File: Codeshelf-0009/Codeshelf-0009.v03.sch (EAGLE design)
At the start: 24 parts, among them U1 MC9S08QG-DT, U2 LED5060A, U3 RS485SOIC, U4 CAT9552

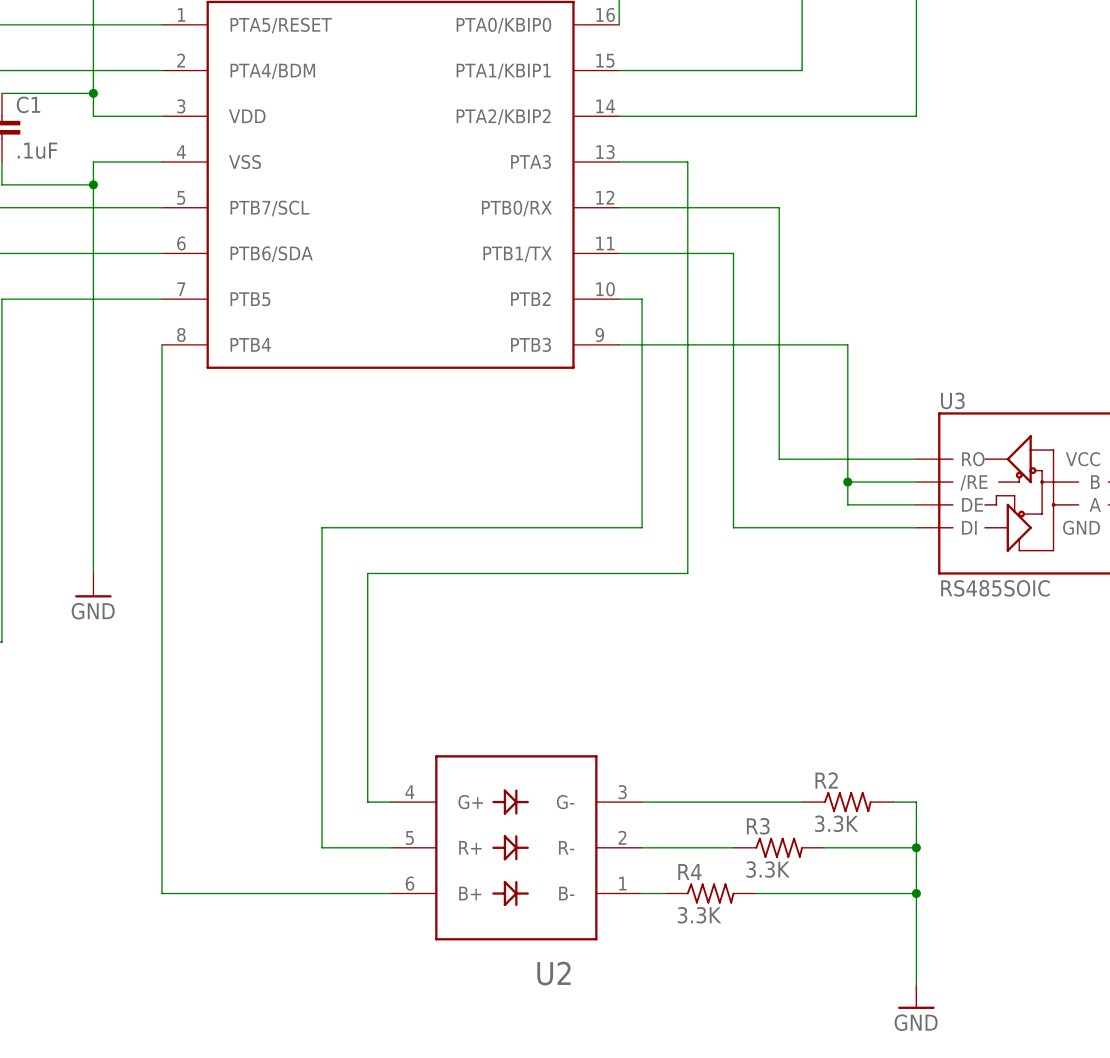
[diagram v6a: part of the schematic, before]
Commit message: Switched LED
Exchanged for WS2812 and reroute to match old PosCon pin assigments for
firmware compatibility.
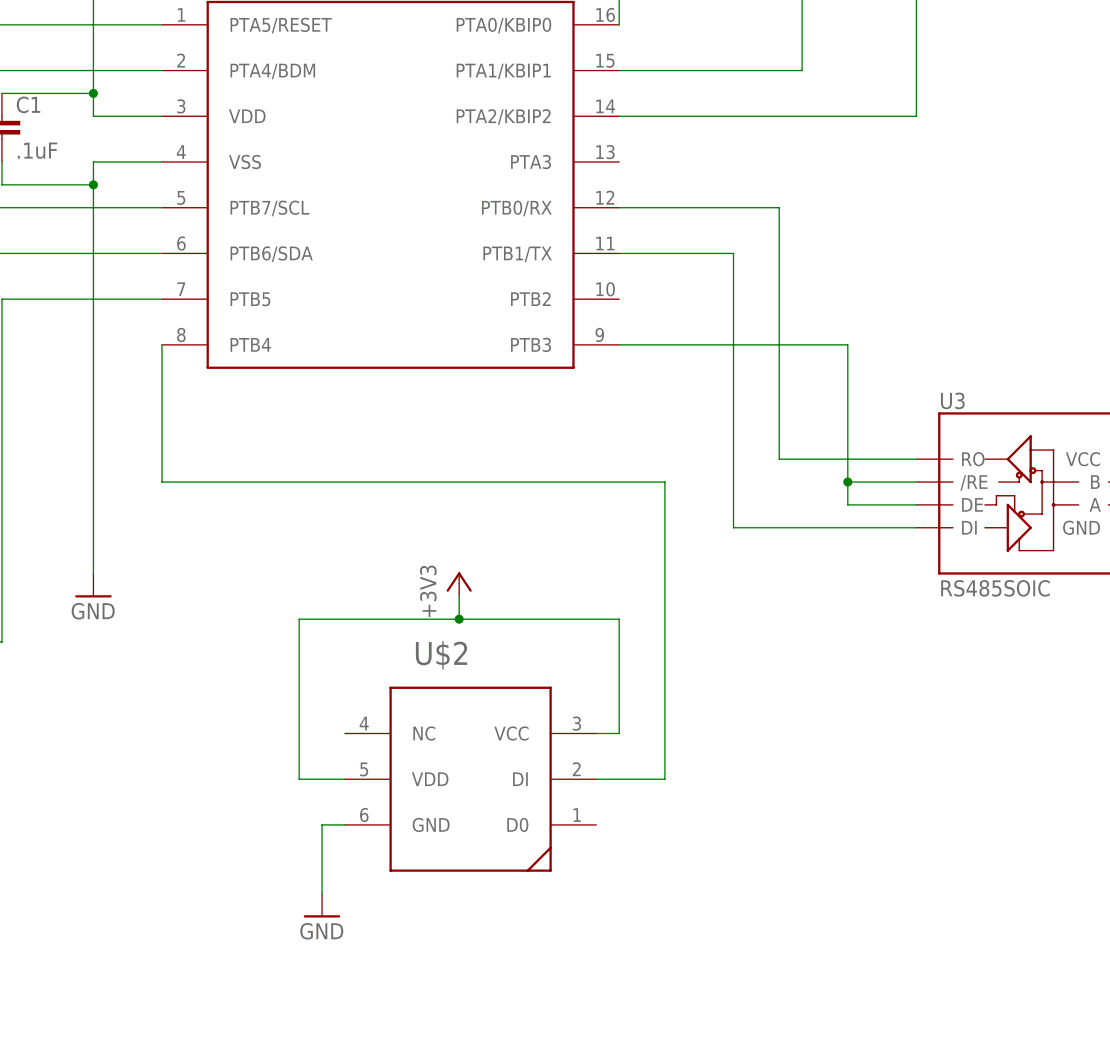
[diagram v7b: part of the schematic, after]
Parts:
- removed R2, R3, R4: 3.3K, GW-devices:RF-R0402
- removed U2: LED5060A, GW-devices:LED5060A
- added U$2: WS2812, GW-devices:WS2812
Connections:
- removed net N$1: R2.1, U2.G-
- removed net N$4: R4.1, U2.B-
- removed net N$5: U1.PTA3, U2.G+
- removed net N$6: U1.PTB2, U2.R+
- removed net N$7: U1.PTB4, U2.B+
- net +3V3: now also U$2.VCC, U$2.VDD
- net GND: now also U$2.GND; no longer R2.2, R3.2, R4.2
- net N$3: now also U$2.DI, U1.PTB4; no longer R3.1, U2.R-
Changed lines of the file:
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@@
 <attribute name="PRICE" value="4.29"/>
 </part>
-<part name="U2" library="GW-devices" deviceset="LED5060" device="A"/>
-<part name="R2" library="GW-devices" deviceset="RF-R" device="0402" value="3.3K">
-<attribute name="MFGN" value="Panasonic"/>
-<attribute name="MFGP" value="ERJ-2GEJ332X"/>
-<attribute name="PRICE" value="0.02"/>
-</part>
-<part name="R3" library="GW-devices" deviceset="RF-R" device="0402" value="3.3K">
-<attribute name="MFGN" value="Panasonic"/>
-<attribute name="MFGP" value="ERJ-2GEJ332X"/>
-<attribute name="PRICE" value="0.02"/>
-</part>
-<part name="R4" library="GW-devices" deviceset="RF-R" device="0402" value="3.3K">
-<attribute name="MFGN" value="Panasonic"/>
-<attribute name="MFGP" value="ERJ-2GEJ332X"/>
-<attribute name="PRICE" value="0.02"/>
-</part>
-<part name="GND2" library="supply1" deviceset="GND" device=""/>
 <part name="U4" library="GW-devices" deviceset="CAT9552" device=""/>
 <part name="GND12" library="supply1" deviceset="GND" device=""/>
@@
 <part name="U$1" library="GW-devices" deviceset="RJ45-8" device=""/>
 <part name="U$2-PROG" library="GW-devices" deviceset="RJ45-8" device=""/>
+<part name="U$2" library="GW-devices" deviceset="WS2812" device=""/>
+<part name="GND2" library="supply1" deviceset="GND" device=""/>
+<part name="+3V7" library="supply1" deviceset="+3V3" device=""/>
 </parts>
 <sheets>
@@
 <attribute name="PRICE" x="68.58" y="-33.02" size="1.778" layer="96" display="off"/>
 </instance>
-<instance part="U2" gate="G$1" x="15.24" y="-73.66" rot="R180"/>
-<instance part="R2" gate="G$1" x="50.8" y="-68.58">
-<attribute name="MFGN" x="50.8" y="-68.58" size="1.778" layer="96" display="off"/>
-<attribute name="MFGP" x="50.8" y="-68.58" size="1.778" layer="96" display="off"/>
-<attribute name="PRICE" x="50.8" y="-68.58" size="1.778" layer="96" display="off"/>
-</instance>
-<instance part="R3" gate="G$1" x="43.18" y="-73.66">
-<attribute name="MFGN" x="43.18" y="-73.66" size="1.778" layer="96" display="off"/>
-<attribute name="MFGP" x="43.18" y="-73.66" size="1.778" layer="96" display="off"/>
-<attribute name="PRICE" x="43.18" y="-73.66" size="1.778" layer="96" display="off"/>
-</instance>
-<instance part="R4" gate="G$1" x="35.56" y="-78.74">
-<attribute name="MFGN" x="35.56" y="-78.74" size="1.778" layer="96" display="off"/>
-<attribute name="MFGP" x="35.56" y="-78.74" size="1.778" layer="96" display="off"/>
-<attribute name="PRICE" x="35.56" y="-78.74" size="1.778" layer="96" display="off"/>
-</instance>
-<instance part="GND2" gate="1" x="58.42" y="-91.44"/>
 <instance part="U4" gate="G$1" x="-134.62" y="81.28" rot="R270"/>
 <instance part="GND12" gate="1" x="-111.76" y="111.76" rot="R180"/>
@@
 <instance part="U$1" gate="G$1" x="170.18" y="-20.32"/>
 <instance part="U$2-PROG" gate="G$1" x="170.18" y="-66.04"/>
+<instance part="U$2" gate="G$1" x="10.16" y="-66.04"/>
+<instance part="GND2" gate="1" x="-7.62" y="-81.28"/>
+<instance part="+3V7" gate="G$1" x="7.62" y="-43.18"/>
 </instances>
 <busses>
@@
 <pinref part="BDM" gate="G$1" pin="8"/>
 <wire x1="-83.82" y1="25.4" x2="-71.12" y2="25.4" width="0.1524" layer="91"/>
-</segment>
-<segment>
-<wire x1="55.88" y1="-68.58" x2="58.42" y2="-68.58" width="0.1524" layer="91"/>
-<wire x1="58.42" y1="-68.58" x2="58.42" y2="-73.66" width="0.1524" layer="91"/>
-<wire x1="58.42" y1="-73.66" x2="58.42" y2="-78.74" width="0.1524" layer="91"/>
-<wire x1="58.42" y1="-78.74" x2="58.42" y2="-88.9" width="0.1524" layer="91"/>
-<wire x1="48.26" y1="-73.66" x2="58.42" y2="-73.66" width="0.1524" layer="91"/>
-<wire x1="40.64" y1="-78.74" x2="58.42" y2="-78.74" width="0.1524" layer="91"/>
-<junction x="58.42" y="-73.66"/>
-<junction x="58.42" y="-78.74"/>
-<pinref part="R2" gate="G$1" pin="2"/>
-<pinref part="GND2" gate="1" pin="GND"/>
-<pinref part="R3" gate="G$1" pin="2"/>
-<pinref part="R4" gate="G$1" pin="2"/>
 </segment>
 <segment>
@@
 <pinref part="U$4" gate="G$1" pin="4"/>
 </segment>
+<segment>
+<pinref part="U$2" gate="G$1" pin="GND"/>
+<pinref part="GND2" gate="1" pin="GND"/>
+<wire x1="-5.08" y1="-71.12" x2="-7.62" y2="-71.12" width="0.1524" layer="91"/>
+<wire x1="-7.62" y1="-71.12" x2="-7.62" y2="-78.74" width="0.1524" layer="91"/>
+</segment>
 </net>
 <net name="+3V3" class="1">
@@
 <wire x1="-307.34" y1="104.14" x2="-307.34" y2="106.68" width="0.1524" layer="91"/>
 </segment>
+<segment>
+<pinref part="U$2" gate="G$1" pin="VDD"/>
+<wire x1="-5.08" y1="-66.04" x2="-10.16" y2="-66.04" width="0.1524" layer="91"/>
+<wire x1="-10.16" y1="-66.04" x2="-10.16" y2="-48.26" width="0.1524" layer="91"/>
+<wire x1="-10.16" y1="-48.26" x2="7.62" y2="-48.26" width="0.1524" layer="91"/>
+<wire x1="7.62" y1="-48.26" x2="25.4" y2="-48.26" width="0.1524" layer="91"/>
+<wire x1="25.4" y1="-48.26" x2="25.4" y2="-60.96" width="0.1524" layer="91"/>
+<pinref part="U$2" gate="G$1" pin="VCC"/>
+<wire x1="25.4" y1="-60.96" x2="22.86" y2="-60.96" width="0.1524" layer="91"/>
+<pinref part="+3V7" gate="G$1" pin="+3V3"/>
+<wire x1="7.62" y1="-45.72" x2="7.62" y2="-48.26" width="0.1524" layer="91"/>
+<junction x="7.62" y="-48.26"/>
+</segment>
 </net>
 <net name="TX" class="0">
@@
 <pinref part="U$1" gate="G$1" pin="5"/>
 <pinref part="U$2-PROG" gate="G$1" pin="5"/>
-</segment>
-</net>
-<net name="N$1" class="0">
-<segment>
-<wire x1="27.94" y1="-68.58" x2="45.72" y2="-68.58" width="0.1524" layer="91"/>
-<pinref part="U2" gate="G$1" pin="G-"/>
-<pinref part="R2" gate="G$1" pin="1"/>
-</segment>
-</net>
-<net name="N$3" class="0">
-<segment>
-<wire x1="27.94" y1="-73.66" x2="38.1" y2="-73.66" width="0.1524" layer="91"/>
-<pinref part="U2" gate="G$1" pin="R-"/>
-<pinref part="R3" gate="G$1" pin="1"/>
-</segment>
-</net>
-<net name="N$4" class="0">
-<segment>
-<wire x1="27.94" y1="-78.74" x2="30.48" y2="-78.74" width="0.1524" layer="91"/>
-<pinref part="U2" gate="G$1" pin="B-"/>
-<pinref part="R4" gate="G$1" pin="1"/>
-</segment>
-</net>
-<net name="N$5" class="0">
-<segment>
-<wire x1="-2.54" y1="-68.58" x2="0" y2="-68.58" width="0.1524" layer="91"/>
-<pinref part="U2" gate="G$1" pin="G+"/>
-<wire x1="-2.54" y1="-68.58" x2="-2.54" y2="-43.18" width="0.1524" layer="91"/>
-<wire x1="-2.54" y1="-43.18" x2="33.02" y2="-43.18" width="0.1524" layer="91"/>
-<wire x1="33.02" y1="-43.18" x2="33.02" y2="2.54" width="0.1524" layer="91"/>
-<pinref part="U1" gate="G$1" pin="PTA3"/>
-<wire x1="33.02" y1="2.54" x2="25.4" y2="2.54" width="0.1524" layer="91"/>
-</segment>
-</net>
-<net name="N$6" class="0">
-<segment>
-<wire x1="-7.62" y1="-73.66" x2="0" y2="-73.66" width="0.1524" layer="91"/>
-<pinref part="U2" gate="G$1" pin="R+"/>
-<pinref part="U1" gate="G$1" pin="PTB2"/>
-<wire x1="25.4" y1="-12.7" x2="27.94" y2="-12.7" width="0.1524" layer="91"/>
-<wire x1="27.94" y1="-12.7" x2="27.94" y2="-38.1" width="0.1524" layer="91"/>
-<wire x1="27.94" y1="-38.1" x2="-7.62" y2="-38.1" width="0.1524" layer="91"/>
-<wire x1="-7.62" y1="-38.1" x2="-7.62" y2="-73.66" width="0.1524" layer="91"/>
-</segment>
-</net>
-<net name="N$7" class="0">
-<segment>
-<pinref part="U2" gate="G$1" pin="B+"/>
-<pinref part="U1" gate="G$1" pin="PTB4"/>
-<wire x1="0" y1="-78.74" x2="-25.4" y2="-78.74" width="0.1524" layer="91"/>
-<wire x1="-25.4" y1="-78.74" x2="-25.4" y2="-17.78" width="0.1524" layer="91"/>
 </segment>
 </net>
@@
 </segment>
 </net>
+<net name="N$3" class="0">
+<segment>
+<pinref part="U$2" gate="G$1" pin="DI"/>
+<wire x1="22.86" y1="-66.04" x2="30.48" y2="-66.04" width="0.1524" layer="91"/>
+<wire x1="30.48" y1="-66.04" x2="30.48" y2="-33.02" width="0.1524" layer="91"/>
+<pinref part="U1" gate="G$1" pin="PTB4"/>
+<wire x1="30.48" y1="-33.02" x2="-25.4" y2="-33.02" width="0.1524" layer="91"/>
+<wire x1="-25.4" y1="-33.02" x2="-25.4" y2="-17.78" width="0.1524" layer="91"/>
+</segment>
+</net>
